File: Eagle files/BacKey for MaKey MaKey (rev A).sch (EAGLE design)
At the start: 5 parts

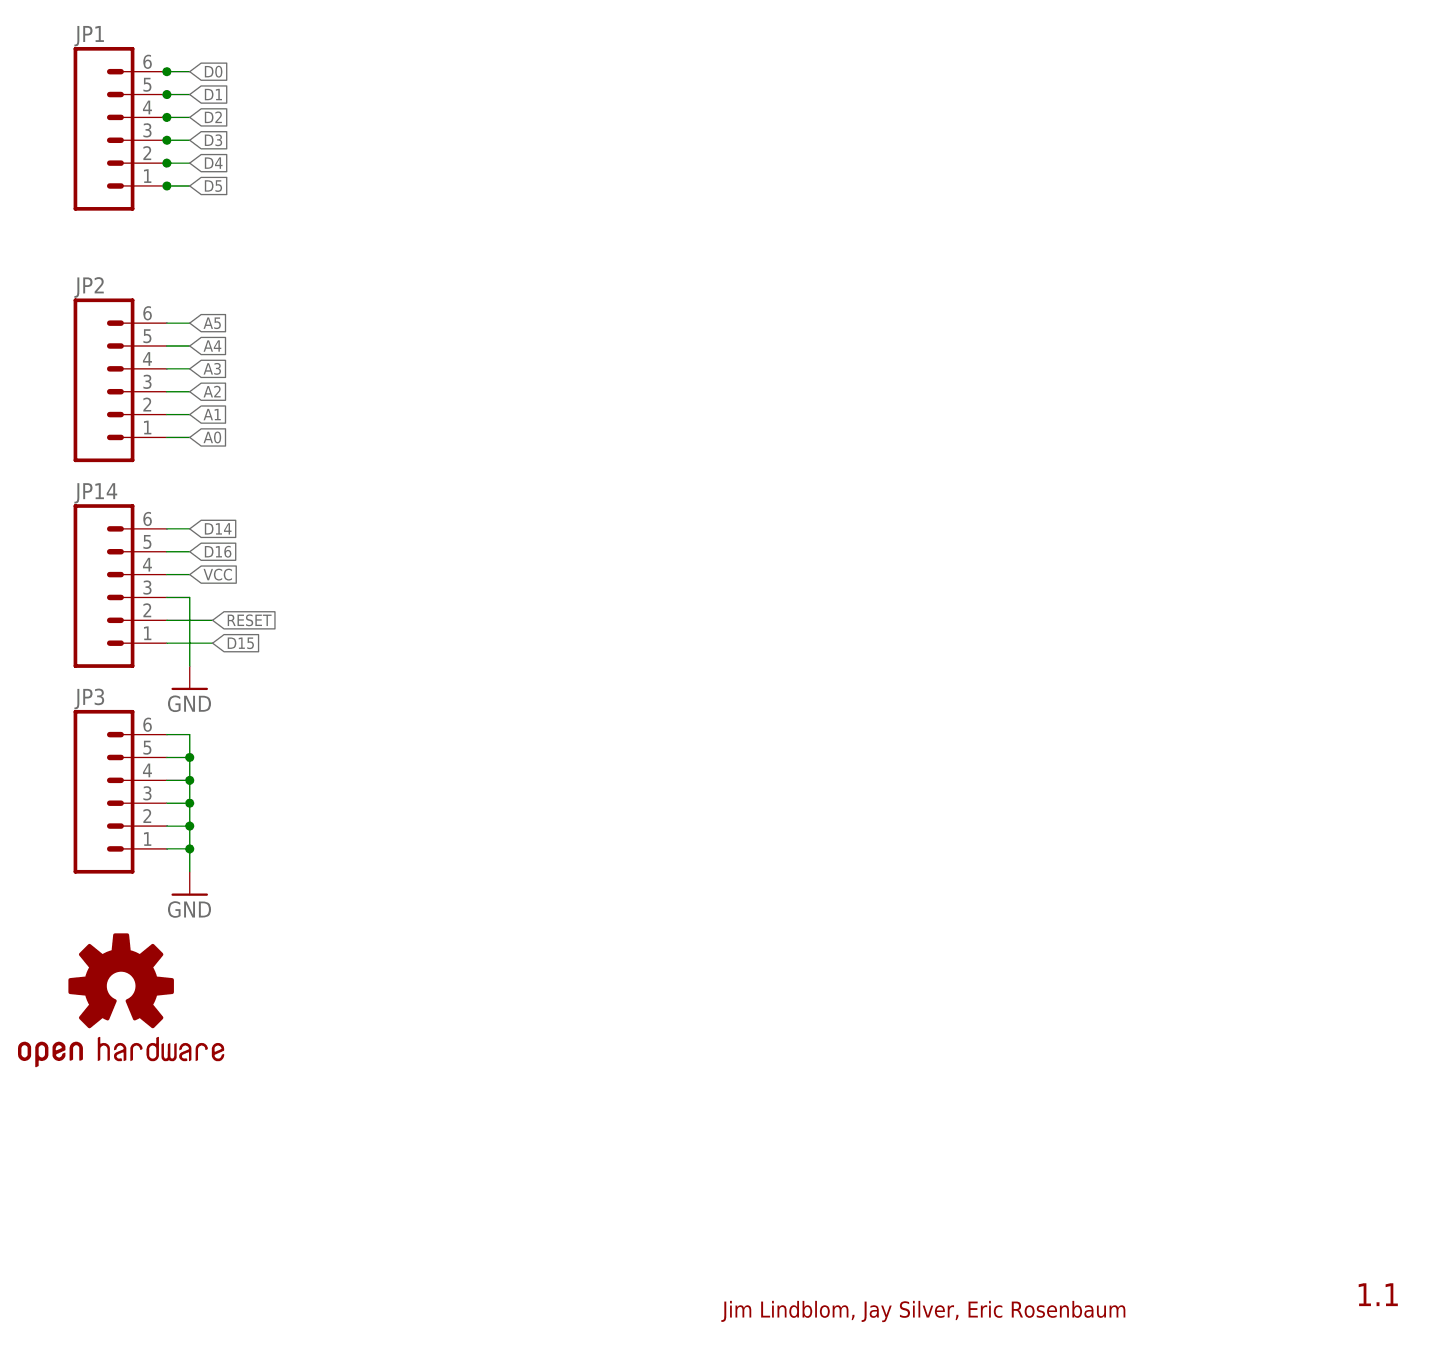
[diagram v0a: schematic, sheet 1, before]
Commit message: Cleaned up schematic a bit
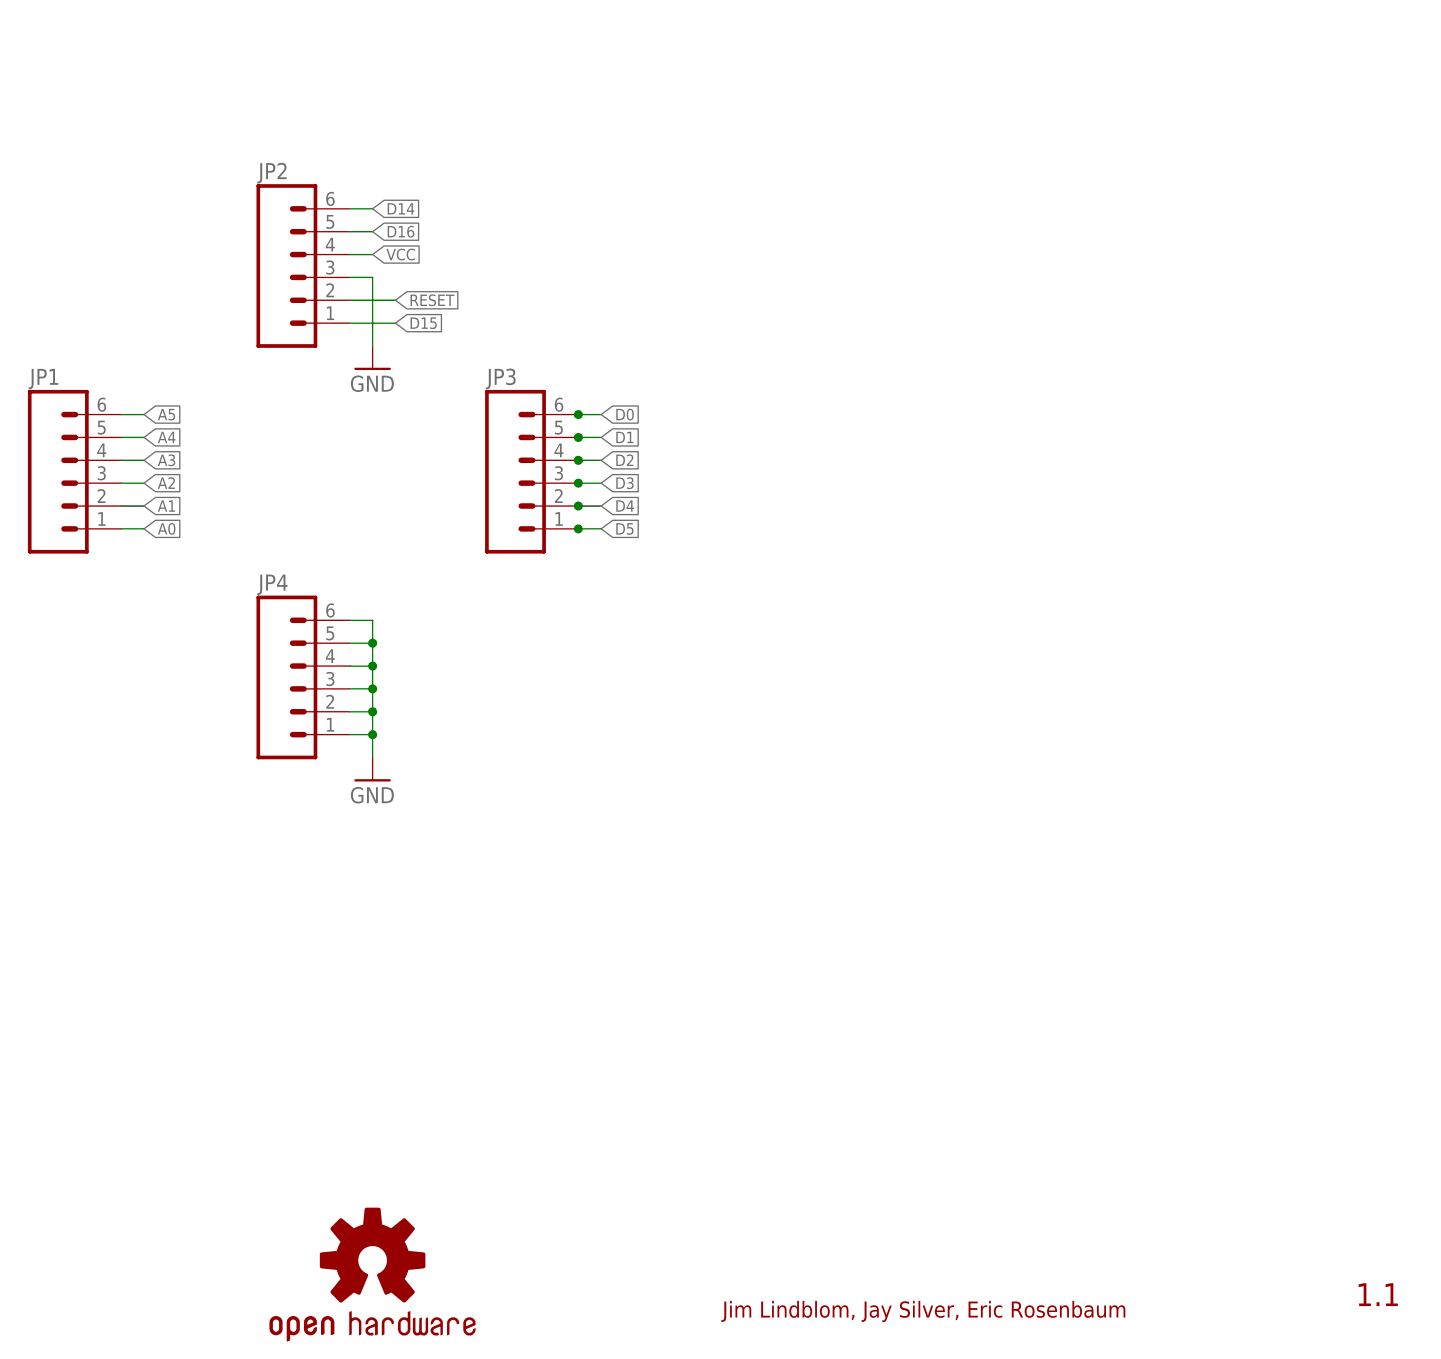
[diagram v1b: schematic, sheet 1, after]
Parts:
- removed JP14: (no value), SparkFun-Connectors:M06SIP
- added JP4: (no value), SparkFun-Connectors:M06SIP
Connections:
- net A0: now also JP1.1; no longer JP2.1
- net A1: now also JP1.2; no longer JP2.2
- net A2: now also JP1.3; no longer JP2.3
- net A3: now also JP1.4; no longer JP2.4
- net A4: now also JP1.5; no longer JP2.5
- net A5: now also JP1.6; no longer JP2.6
- net D0: now also JP3.6; no longer JP1.6
- net D1: now also JP3.5; no longer JP1.5
- net D14: now also JP2.6; no longer JP14.6
- net D15: now also JP2.1; no longer JP14.1
- net D16: now also JP2.5; no longer JP14.5
- net D2: now also JP3.4; no longer JP1.4
- net D3: now also JP3.3; no longer JP1.3
- net D4: now also JP3.2; no longer JP1.2
- net D5: now also JP3.1; no longer JP1.1
- net GND: now also JP2.3, JP4.1, JP4.2, JP4.3, JP4.4, JP4.5, JP4.6; no longer JP14.3, JP3.1, JP3.2, JP3.3, JP3.4, JP3.5, JP3.6
- net RESET: now also JP2.2; no longer JP14.2
- net VCC: now also JP2.4; no longer JP14.4
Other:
- moved on the sheet: JP1, JP2, JP3
